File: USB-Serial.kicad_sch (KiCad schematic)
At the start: 6 parts, among them U12 CH340C

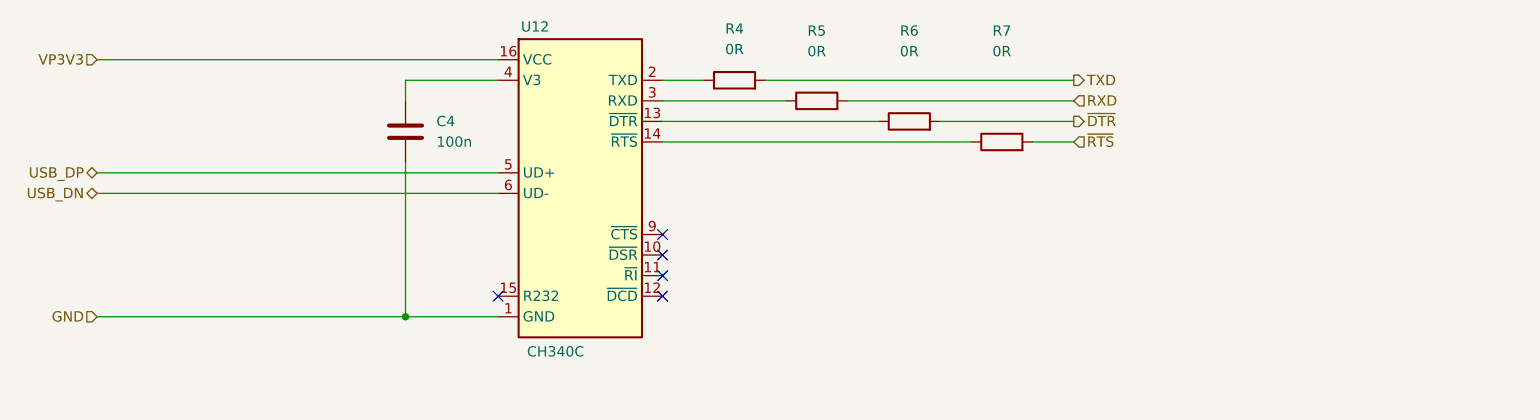
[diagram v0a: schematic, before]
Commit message: Ethernet progress, 40pin connector, save progress
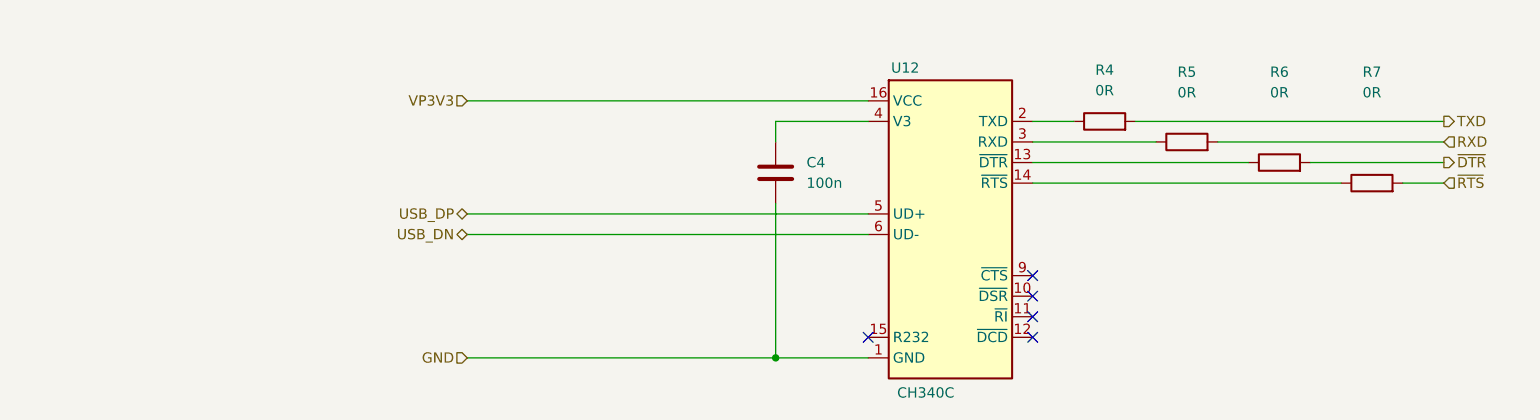
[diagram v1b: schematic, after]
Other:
- moved on the sheet: C4, R4, R5, R6, R7, U12

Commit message: Layout save
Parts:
- C4: footprint (none) -> Capacitor_SMD:C_0603_1608Metric
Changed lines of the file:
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@@
 			)
 		)
-		(property "Footprint" ""
+		(property "Footprint" "Capacitor_SMD:C_0603_1608Metric"
 			(at 130.5052 88.9 0)
 			(hide yes)

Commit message: Power layout started
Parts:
- R4, R5, R6, R7: footprint Resistor_SMD:R_0201_0603Metric -> Resistor_SMD:R_0603_1608Metric
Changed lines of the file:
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@@
 			)
 		)
-		(property "Footprint" "Resistor_SMD:R_0201_0603Metric"
+		(property "Footprint" "Resistor_SMD:R_0603_1608Metric"
 			(at 203.2 88.138 90)
 			(hide yes)
@@
 			)
 		)
-		(property "Footprint" "Resistor_SMD:R_0201_0603Metric"
+		(property "Footprint" "Resistor_SMD:R_0603_1608Metric"
 			(at 191.77 85.598 90)
 			(hide yes)
@@
 			)
 		)
-		(property "Footprint" "Resistor_SMD:R_0201_0603Metric"
+		(property "Footprint" "Resistor_SMD:R_0603_1608Metric"
 			(at 180.34 83.058 90)
 			(hide yes)
@@
 			)
 		)
-		(property "Footprint" "Resistor_SMD:R_0201_0603Metric"
+		(property "Footprint" "Resistor_SMD:R_0603_1608Metric"
 			(at 170.18 80.518 90)
 			(hide yes)
